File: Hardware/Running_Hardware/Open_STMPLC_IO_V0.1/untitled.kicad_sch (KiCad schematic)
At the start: 26 parts, among them J1 Screw_Terminal_01x02, Q1 SUD50P06, Q2 AO3400A, U7 TPS26600PWP, U8 UCC23513

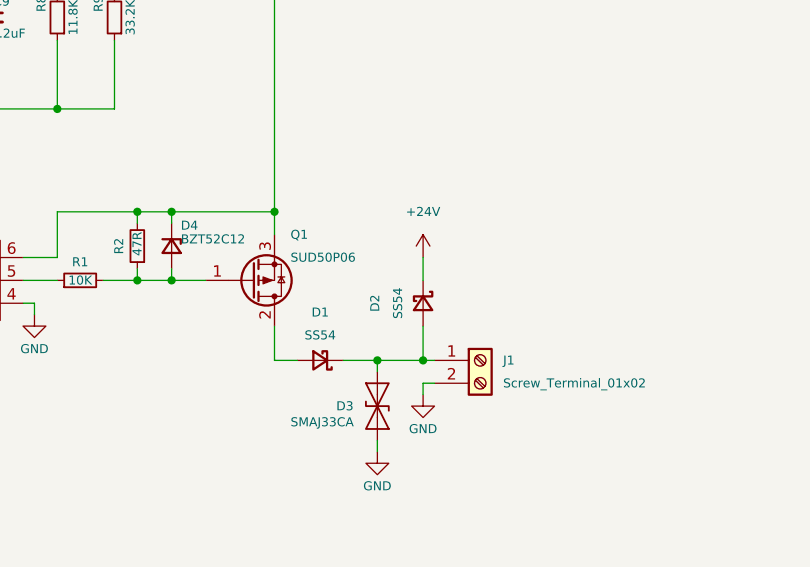
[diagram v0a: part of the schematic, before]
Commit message: IO board schematic changes
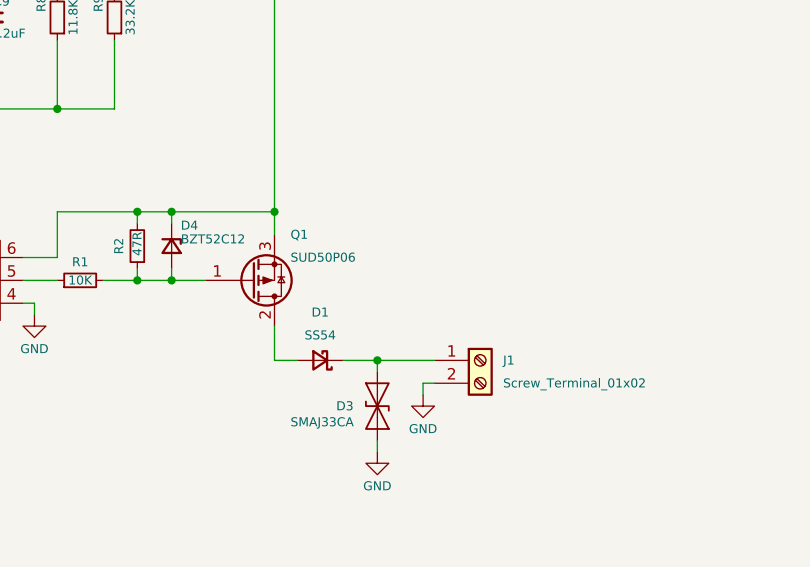
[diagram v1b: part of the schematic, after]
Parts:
- removed D2: SS54, symbol Device:D_Schottky_Small
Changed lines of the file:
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@@
-	)
-	(junction
-		(at 199.39 121.92)
-		(diameter 0)
-		(color 0 0 0 0)
 	)
 	(junction
@@
 	(wire
 		(pts
-			(xy 199.39 121.92) (xy 200.66 121.92)
+			(xy 194.31 121.92) (xy 200.66 121.92)
 		)
 		(stroke
@@
 	(wire
 		(pts
-			(xy 199.39 118.11) (xy 199.39 121.92)
-		)
-		(stroke
-			(width 0)
-			(type default)
-		)
-	)
-	(wire
-		(pts
 			(xy 125.73 115.57) (xy 127 115.57)
 		)
@@
 	(wire
 		(pts
-			(xy 199.39 110.49) (xy 199.39 113.03)
-		)
-		(stroke
-			(width 0)
-			(type default)
-		)
-	)
-	(wire
-		(pts
 			(xy 106.68 123.19) (xy 107.95 123.19)
 		)
@@
 		(pts
 			(xy 199.39 124.46) (xy 200.66 124.46)
-		)
-		(stroke
-			(width 0)
-			(type default)
-		)
-	)
-	(wire
-		(pts
-			(xy 194.31 121.92) (xy 199.39 121.92)
 		)
 		(stroke
@@
 	)
 	(symbol
-		(lib_id "power:+24V")
-		(at 199.39 110.49 0)
-		(unit 1)
-		(exclude_from_sim no)
-		(in_bom yes)
-		(on_board yes)
-		(dnp no)
-		(fields_autoplaced yes)
-		(property "Reference" "#PWR010"
-			(at 199.39 114.3 0)
-			(effects
-				(font
-					(size 1 1)
-				)
-				(hide yes)
-			)
-		)
-		(property "Value" "+24V"
-			(at 199.39 105.41 0)
-			(effects
-				(font
-					(size 1 1)
-				)
-			)
-		)
-		(property "Footprint" ""
-			(at 199.39 110.49 0)
-			(effects
-				(font
-					(size 1.27 1.27)
-				)
-				(hide yes)
-			)
-		)
-		(property "Datasheet" ""
-			(at 199.39 110.49 0)
-			(effects
-				(font
-					(size 1.27 1.27)
-				)
-				(hide yes)
-			)
-		)
-		(property "Description" "Power symbol creates a global label with name \"+24V\""
-			(at 199.39 110.49 0)
-			(effects
-				(font
-					(size 1.27 1.27)
-				)
-				(hide yes)
-			)
-		)
-		(pin "1"
-		)
-		(instances
-			(project "Open_STMPLC_IO_V0.1"
-				(path "/4d6787b6-1f4f-4098-b70b-d936e584350b/14439578-ba67-46a0-8d60-ec0dac961d93"
-					(reference "#PWR010")
-					(unit 1)
-				)
-			)
-		)
-	)
-	(symbol
 		(lib_id "Device:C_Small")
 		(at 105.41 59.69 0)
@@
 					(unit 1)
 				)
-			)
-		)
-	)
-	(symbol
-		(lib_id "Device:D_Schottky_Small")
-		(at 199.39 115.57 270)
-		(unit 1)
-		(exclude_from_sim no)
-		(in_bom yes)
-		(on_board yes)
-		(dnp no)
-		(property "Reference" "D2"
-			(at 194.056 115.57 0)
-			(effects
-				(font
-					(size 1 1)
-				)
-			)
-		)
-		(property "Value" "SS54"
-			(at 196.596 115.57 0)
-			(effects
-				(font
-					(size 1 1)
-				)
-			)
-		)
-		(property "Footprint" ""
-			(at 199.39 115.57 90)
-			(effects
-				(font
-					(size 1.27 1.27)
-				)
-				(hide yes)
-			)
-		)
-		(property "Datasheet" "~"
-			(at 199.39 115.57 90)
-			(effects
-				(font
-					(size 1.27 1.27)
-				)
-				(hide yes)
-			)
-		)
-		(property "Description" "Schottky diode, small symbol"
-			(at 199.39 115.57 0)
-			(effects
-				(font
-					(size 1.27 1.27)
-				)
-				(hide yes)
-			)
-		)
-		(pin "1"
-		)
-		(pin "2"
-		)
-		(instances
-			(project "Open_STMPLC_IO_V0.1"
-				(path "/4d6787b6-1f4f-4098-b70b-d936e584350b/14439578-ba67-46a0-8d60-ec0dac961d93"
-					(reference "D2")
-					(unit 1)
-				)
